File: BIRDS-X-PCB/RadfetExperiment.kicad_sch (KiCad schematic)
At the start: 34 parts, among them U301 VT03, U302 VT03, U303 VT03, U304 VT03, U305 TL974IPWR, U306 ADG734, U308 LM334M, U309 LM334M, U310 LM334M, U311 LM334M

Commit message: Prep docs for Rev5.1 release
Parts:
- JP301: now not fitted; now left out of the parts list
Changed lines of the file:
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@@
   (paper "USLetter")
   (title_block
-    (rev "Rev5.0")
+    (date "2023-09-07")
+    (rev "Rev5.1")
   )
   (junction (at 209.55 121.92) (diameter 0) (color 0 0 0 0)
@@
   )
   (symbol (lib_id "Jumper:Jumper_2_Open") (at 64.77 59.69 0) (unit 1)
-    (in_bom yes) (on_board yes) (dnp no)
+    (in_bom no) (on_board yes) (dnp yes)
     (property "Reference" "JP301" (at 64.77 57.15 0)
       (effects (font (size 1.27 1.27)))

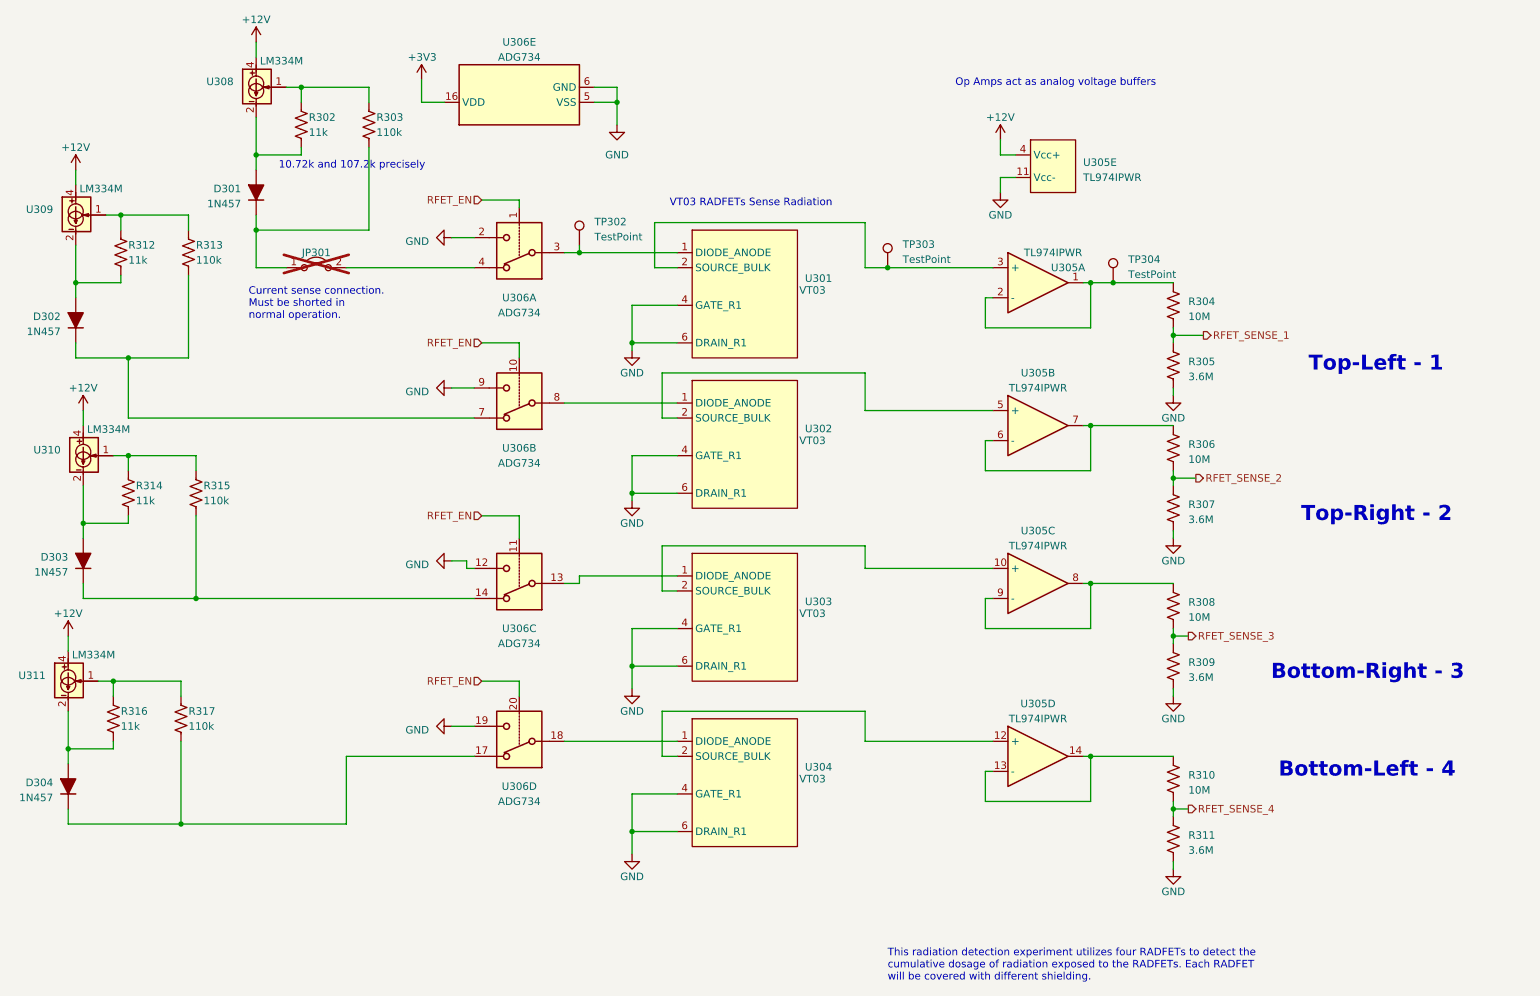
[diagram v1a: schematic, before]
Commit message: Schematic re-work (esp. RADFET fixes)
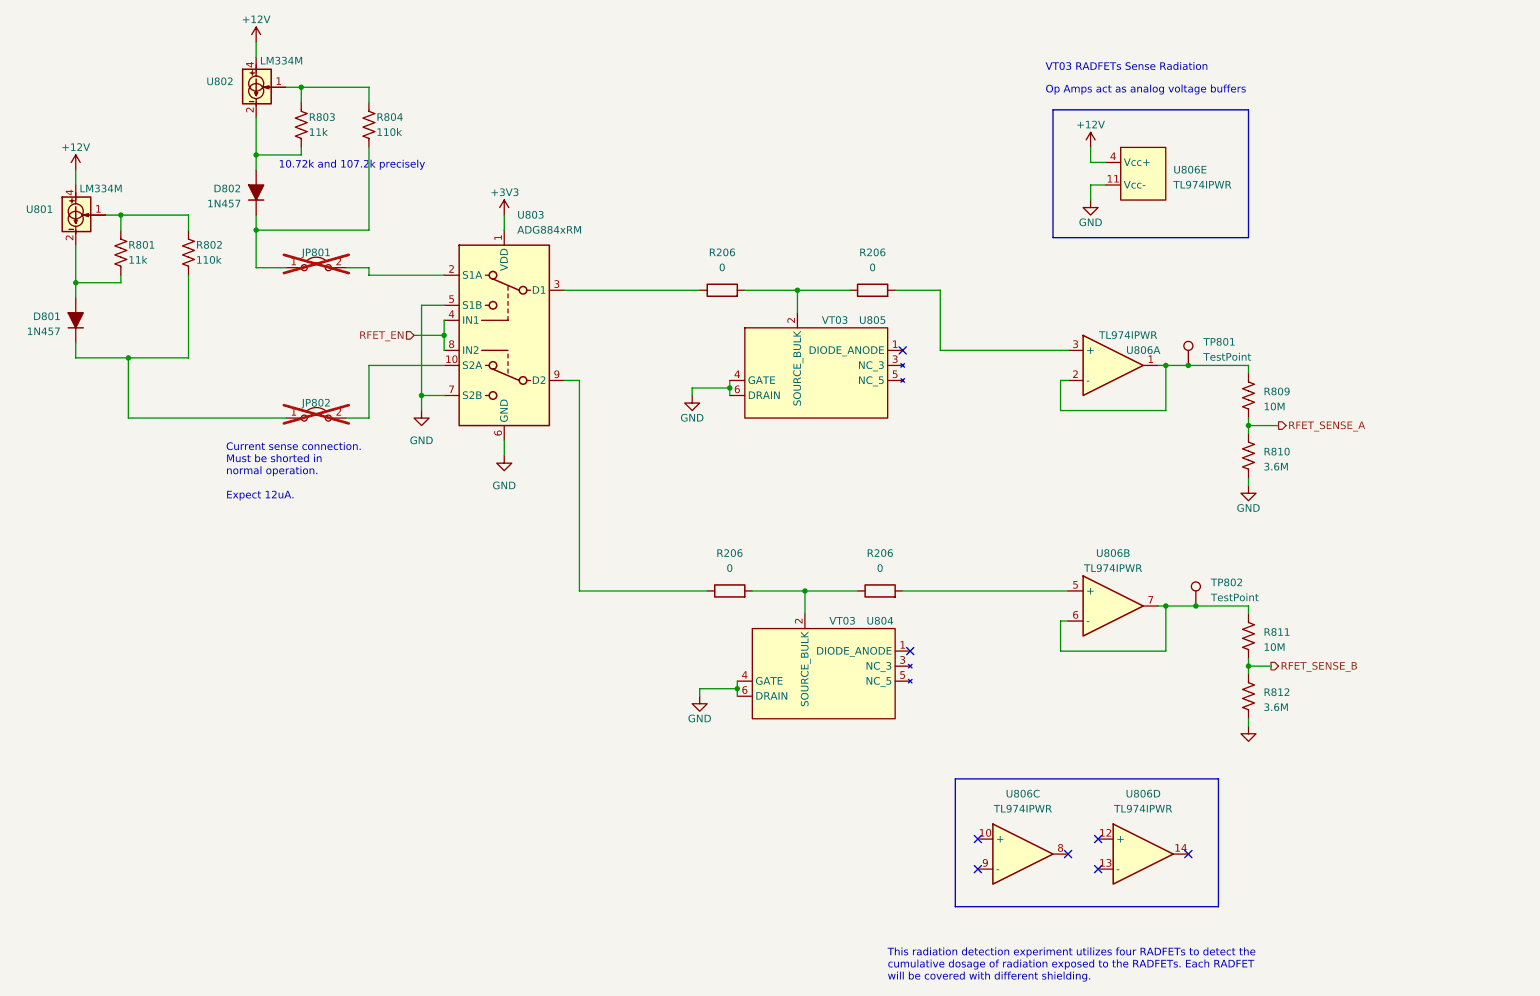
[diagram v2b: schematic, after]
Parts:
- removed D303, D304: 1N457, Diode_THT:D_DO-35_SOD27_P7.62mm_Horizontal, symbol BIRDS-X_Symbols_Lib:1N457
- removed R308, R310: 10M, Resistor_SMD:R_0603_1608Metric_Pad0.98x0.95mm_HandSolder, symbol Device:R_US
- removed R309, R311: 3.6M, Resistor_SMD:R_0603_1608Metric_Pad0.98x0.95mm_HandSolder, symbol Device:R_US
- removed R314, R316: 11k, Resistor_SMD:R_0603_1608Metric_Pad0.98x0.95mm_HandSolder, symbol Device:R_US
- removed R315, R317: 110k, Resistor_SMD:R_0603_1608Metric_Pad0.98x0.95mm_HandSolder, symbol Device:R_US
- removed TP302, TP303: TestPoint, TestPoint:TestPoint_Pad_D1.5mm, symbol Connector:TestPoint
- removed U302, U303, U304: VT03, Package_TO_SOT_SMD:SOT-23-6_Handsoldering, symbol BIRDS-X_Symbols_Lib:VT03_Radfet
- removed unit 3 of U305
- removed unit 4 of U305
- removed U306: ADG734, Package_SO:TSSOP-20_4.4x6.5mm_P0.65mm, symbol Analog_Switch:ADG734
- removed U310, U311: LM334M, Package_SO:SOIC-8_3.9x4.9mm_P1.27mm, symbol BIRDS-X_Symbols_Lib:LM334M
- added JP802: Jumper_2_Open, Connector_PinHeader_1.27mm:PinHeader_1x02_P1.27mm_Vertical, symbol Jumper:Jumper_2_Open
- added R206 (x4): 0, Resistor_SMD:R_0603_1608Metric_Pad0.98x0.95mm_HandSolder, symbol Device:R
- added TP802: TestPoint, TestPoint:TestPoint_Pad_D1.5mm, symbol Connector:TestPoint
- added U803: ADG884xRM, Package_SO:MSOP-10_3x3mm_P0.5mm, symbol Analog_Switch:ADG884xRM
- added U804: VT03, Package_TO_SOT_SMD:SOT-23-6_Handsoldering, symbol BIRDS-X_Symbols_Lib:VT03_Radfet
- added unit 3 of U806
- added unit 4 of U806
- U806: renamed from U305; LCSC (none) -> C544297
- renumbered D302 to D801, D301 to D802, JP301 to JP801, R312 to R801, R313 to R802, R302 to R803, R303 to R804, R304 to R809, R305 to R810, R306 to R811, R307 to R812, TP304 to TP801, U309 to U801, U308 to U802, U301 to U805
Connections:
- net +3V3: now also U803.1 (VDD)
- net GND: now also U803.5 (S1B), U803.6 (GND), U803.7 (S2B), U804.4 (GATE), U804.6 (DRAIN)
- net RFET_EN: now also U803.4 (IN1), U803.8 (IN2)
- net at U806.5 (+): now also R206.2
- net at R811.1, U806.6 (-), U806.7: now also TP802.1
- net at U805.2 (SOURCE_BULK): now also R206.1, R206.2; no longer U806.3 (+)
- net at JP801.2 (B): now also U803.2 (S1A)
- net at D801.1 (K), R802.2: now also JP802.1 (A)
- net RFET_SENSE_1 renamed RFET_SENSE_A
- net RFET_SENSE_2 renamed RFET_SENSE_B
- new net: R206.1, U803.9 (D2)
- new net: R206.1, R206.2, U804.2 (SOURCE_BULK)
- new net: JP802.2 (B), U803.10 (S2A)
- new net: R206.1, U803.3 (D1)
- new net: R206.2, U806.3 (+)
- no-connect marks 0 -> 8
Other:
- note added: "Current sense connection. Must be shorted in normal operation. Expect 12uA."
- note removed: "Bottom-Left - 4"
- note removed: "Bottom-Right - 3"
- note removed: "Current sense connection. Must be shorted in normal operation."
- note removed: "Top-Left - 1"
- note removed: "Top-Right - 2"
- moved on the sheet: R809, R810, R811, R812, TP801, U806A, U806B, U806E

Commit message: Layout PCB
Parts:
- removed TP801, TP802: TestPoint, TestPoint:TestPoint_Pad_D1.5mm, symbol Connector:TestPoint
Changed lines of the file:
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@@
   (junction (at 31.75 50.8) (diameter 0) (color 0 0 0 0)
   )
-  (junction (at 212.09 76.2) (diameter 0) (color 0 0 0 0)
-  )
   (junction (at 208.28 116.84) (diameter 0) (color 0 0 0 0)
   )
@@
   )
   (junction (at 134.62 80.01) (diameter 0) (color 0 0 0 0)
-  )
-  (junction (at 213.36 116.84) (diameter 0) (color 0 0 0 0)
   )
   (junction (at 33.02 74.93) (diameter 0) (color 0 0 0 0)
@@
     (stroke (width 0) (type default))
   )
-  (wire (pts (xy 212.09 76.2) (xy 222.25 76.2))
+  (wire (pts (xy 208.28 76.2) (xy 222.25 76.2))
     (stroke (width 0) (type default))
   )
@@
     (stroke (width 0) (type default))
   )
-  (wire (pts (xy 208.28 116.84) (xy 213.36 116.84))
+  (wire (pts (xy 208.28 116.84) (xy 222.25 116.84))
     (stroke (width 0) (type default))
   )
@@
     (stroke (width 0) (type default))
   )
-  (wire (pts (xy 208.28 76.2) (xy 212.09 76.2))
-    (stroke (width 0) (type default))
-  )
   (wire (pts (xy 137.16 63.5) (xy 146.05 63.5))
     (stroke (width 0) (type default))
@@
   )
   (wire (pts (xy 222.25 96.52) (xy 222.25 95.25))
-    (stroke (width 0) (type default))
-  )
-  (wire (pts (xy 213.36 116.84) (xy 222.25 116.84))
     (stroke (width 0) (type default))
   )
@@
     )
   )
-  (symbol (lib_id "Connector:TestPoint") (at 213.36 116.84 0) (unit 1)
-    (in_bom yes) (on_board yes) (dnp no) (fields_autoplaced)
-    (property "Reference" "TP802" (at 215.9 112.903 0)
-      (effects (font (size 1.27 1.27)) (justify left))
-    )
-    (property "Value" "TestPoint" (at 215.9 115.443 0)
-      (effects (font (size 1.27 1.27)) (justify left))
-    )
-    (property "Footprint" "TestPoint:TestPoint_Pad_D1.5mm" (at 218.44 116.84 0)
-      (effects (font (size 1.27 1.27)) hide)
-    )
-    (property "Datasheet" "~" (at 218.44 116.84 0)
-      (effects (font (size 1.27 1.27)) hide)
-    )
-    (pin "1")
-    (instances
-      (project "BIRDS-X-PCB"
-        (path "/c2796b15-795a-4d6e-ad4b-0ba87ded4bc9/adc73a10-1d27-484e-8ce9-d638694b8e29"
-          (reference "TP802") (unit 1)
-        )
-        (path "/c2796b15-795a-4d6e-ad4b-0ba87ded4bc9/4da67a21-a782-4daa-ad81-c58c3b5a549a"
-          (reference "TP902") (unit 1)
-        )
-      )
-    )
-  )
   (symbol (lib_id "Analog_Switch:ADG884xRM") (at 96.52 71.12 0) (unit 1)
     (in_bom yes) (on_board yes) (dnp no) (fields_autoplaced)
@@
         )
       )
-    )
-  )
-  (symbol (lib_id "Connector:TestPoint") (at 212.09 76.2 0) (unit 1)
-    (in_bom yes) (on_board yes) (dnp no) (fields_autoplaced)
-    (property "Reference" "TP801" (at 214.63 72.263 0)
-      (effects (font (size 1.27 1.27)) (justify left))
-    )
-    (property "Value" "TestPoint" (at 214.63 74.803 0)
-      (effects (font (size 1.27 1.27)) (justify left))
-    )
-    (property "Footprint" "TestPoint:TestPoint_Pad_D1.5mm" (at 217.17 76.2 0)
-      (effects (font (size 1.27 1.27)) hide)
-    )
-    (property "Datasheet" "~" (at 217.17 76.2 0)
-      (effects (font (size 1.27 1.27)) hide)
-    )
-    (pin "1")
-    (instances
-      (project "BIRDS-X-PCB"
-        (path "/c2796b15-795a-4d6e-ad4b-0ba87ded4bc9/adc73a10-1d27-484e-8ce9-d638694b8e29"
-          (reference "TP801") (unit 1)
-        )
-        (path "/c2796b15-795a-4d6e-ad4b-0ba87ded4bc9/4da67a21-a782-4daa-ad81-c58c3b5a549a"
-          (reference "TP901") (unit 1)
-        )
-      )
